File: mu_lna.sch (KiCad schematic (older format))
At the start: 60 parts, among them J1 Conn_01x02, J2 Conn_01x02, J3 Conn_01x02, J4 Conn_01x02, J5 Conn_01x01, U1 ADA4523-1, U2 Opamp_Dual_Generic, U3 ADA4523-1, U4 ADA4523-1, U5 ADA4523-1

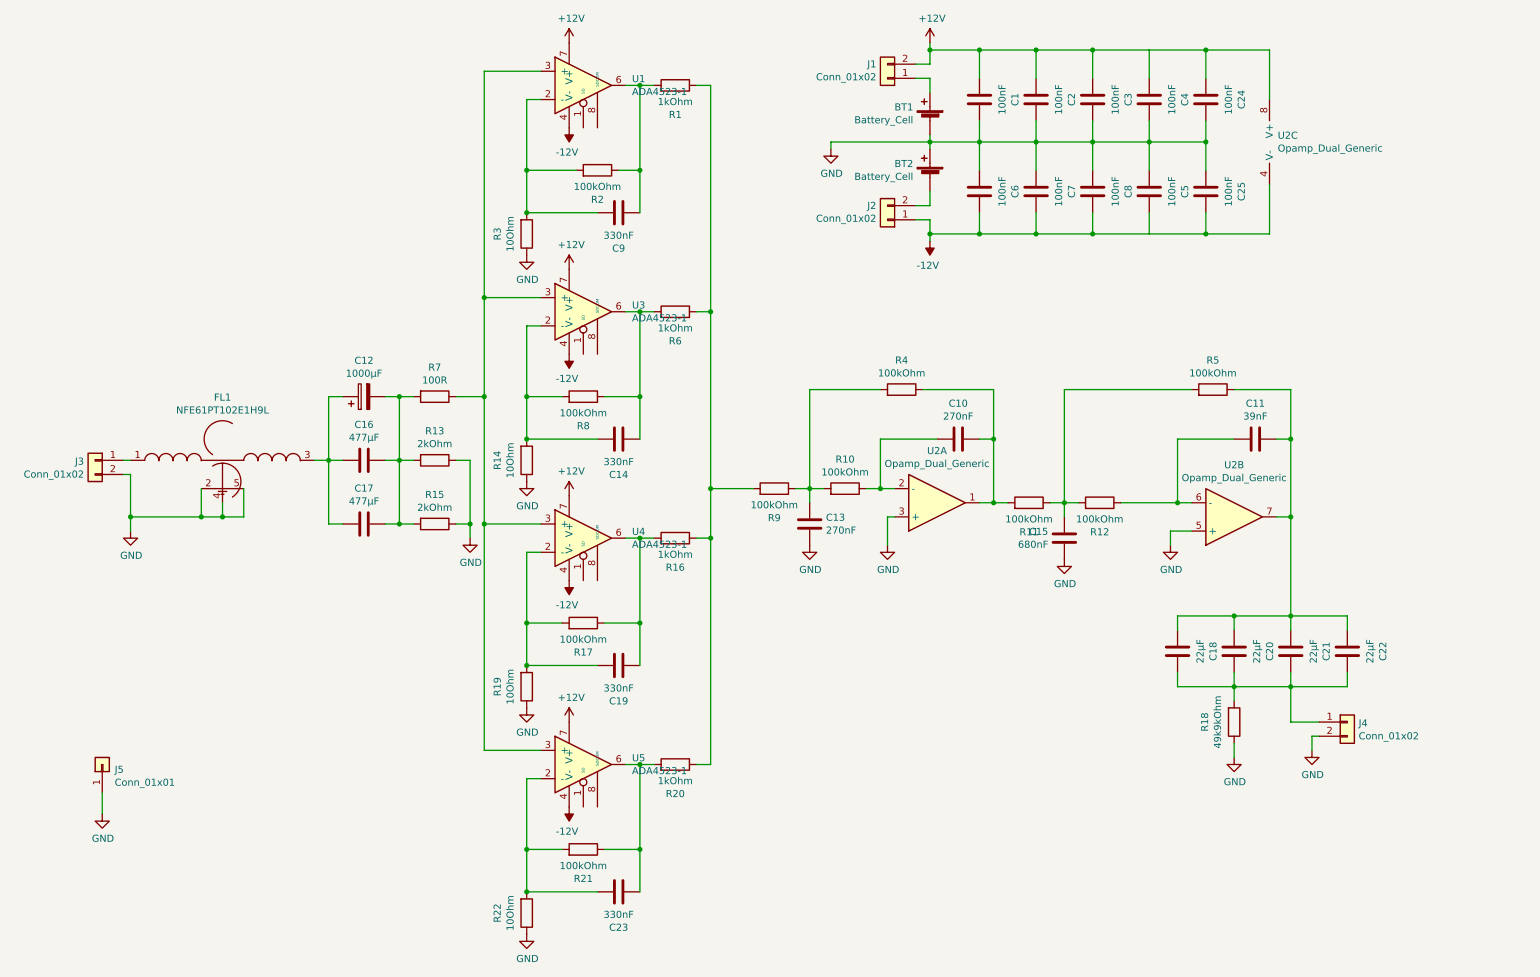
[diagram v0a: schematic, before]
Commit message: new layout for Bopla 84080100
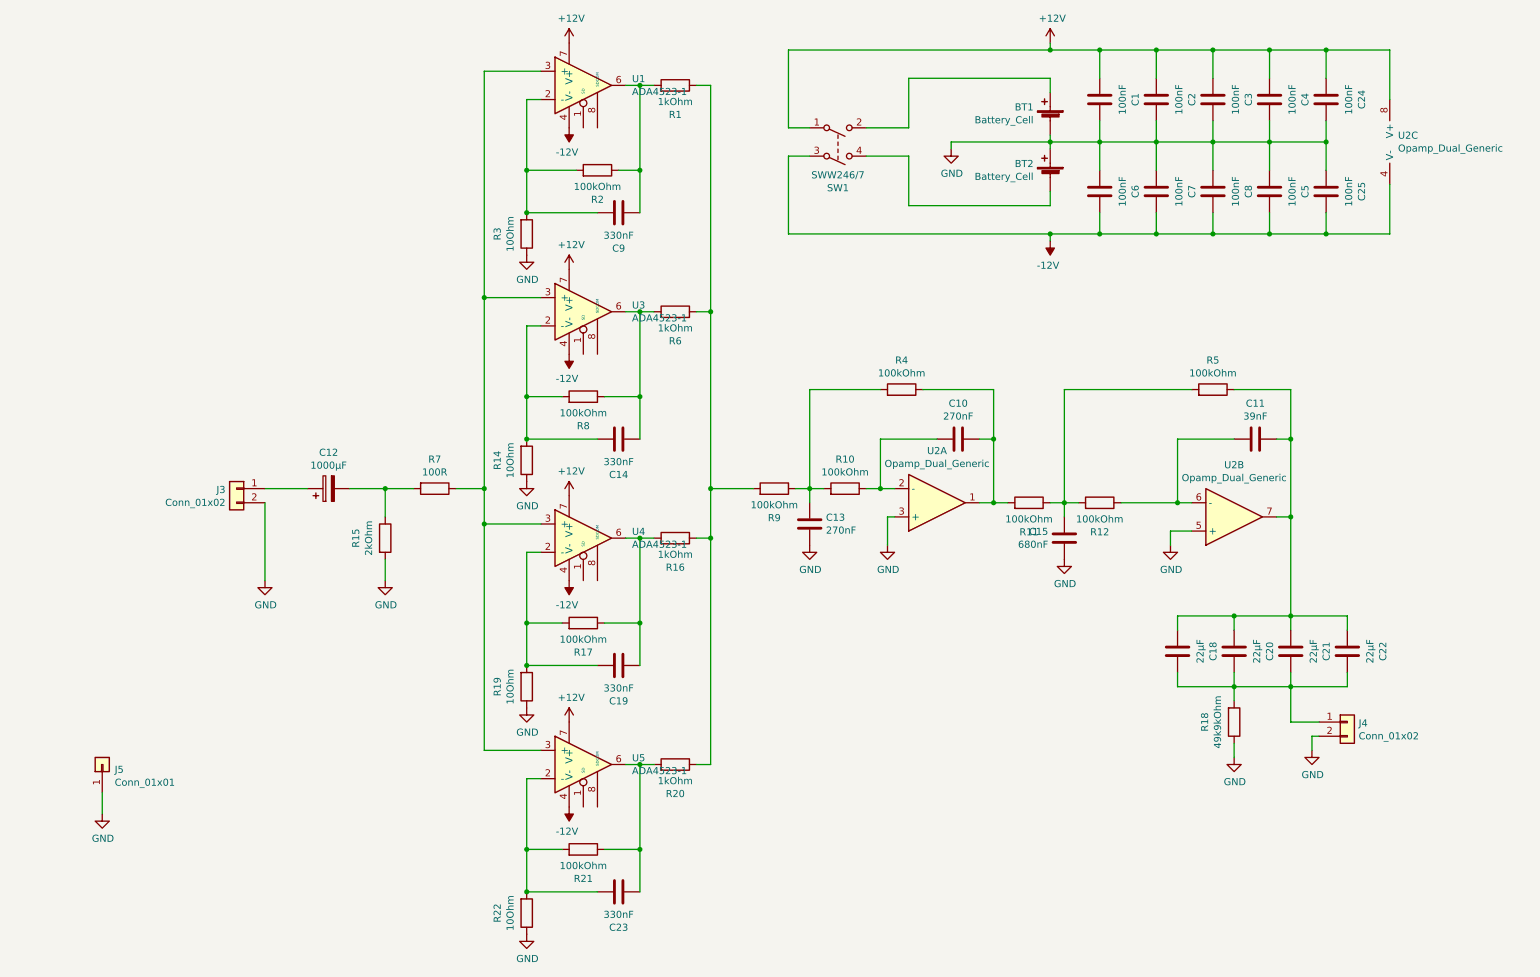
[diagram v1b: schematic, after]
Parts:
- removed C16, C17: 477µF, Capacitor_THT:CP_Axial_L18.0mm_D10.0mm_P25.00mm_Horizontal, symbol Device:C
- removed FL1: NFE61PT102E1H9L, NFE61, symbol SamacSys_Parts:NFE61PT102E1H9L
- removed J1, J2: Conn_01x02, Connector_PinHeader_2.54mm:PinHeader_1x02_P2.54mm_Vertical, symbol Connector_Generic:Conn_01x02
- removed R13: 2kOhm, Resistor_THT:R_Axial_DIN0414_L11.9mm_D4.5mm_P15.24mm_Horizontal, symbol Device:R
- added SW1: SWW246/7, my_lib:RS_DPDT, symbol Switch:SW_DPST
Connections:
- net +12V: now also SW1.1
- net -12V: now also SW1.3
- net GND: now also R15.2; no longer R15.1
- net at BT1.1 (+): now also SW1.2
- net at BT2.2 (-): now also SW1.4
- net at C12.1: now also J3.1 (Pin_1)
- net at C12.2, R7.2: now also R15.1; no longer R15.2
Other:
- moved on the sheet: BT1, BT2, C1, C12, C2, C24, C25, C3, C4, C5, C6, C7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
